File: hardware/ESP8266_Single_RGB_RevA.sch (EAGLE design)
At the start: 41 parts, among them IC1 ESP-12E/F, J1 POWER_JACKPTH_LOCK, J2 B G R +, J4 G S V, Q1 IRF520, Q2 IRF520, Q3 IRF520, T1 2N3904, T2 2N3904, T3 2N3904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

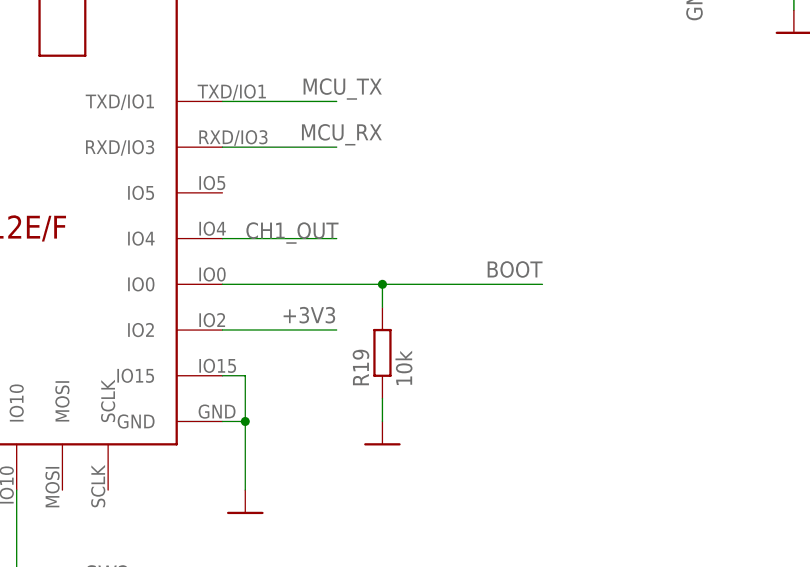
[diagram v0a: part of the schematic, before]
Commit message: fix R16 - NOT NEEDED at ALL
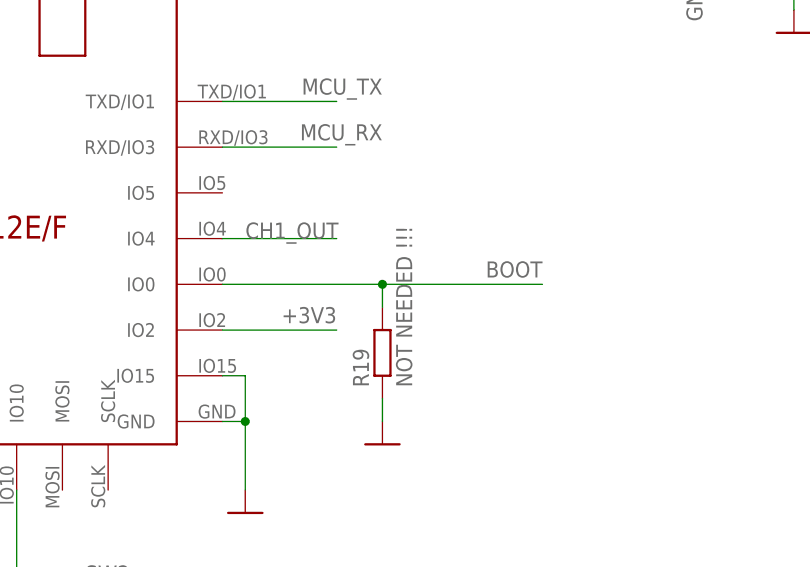
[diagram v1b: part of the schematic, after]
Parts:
- R19: value 10k -> NOT NEEDED !!!
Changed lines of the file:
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@@
 <part name="SV1" library="con-lstb" library_urn="urn:adsk.eagle:library:162" deviceset="MA05-1" device="" package3d_urn="urn:adsk.eagle:package:8332/1" value="GND RX TX BOOT VCC"/>
 <part name="GND31" library="supply1" library_urn="urn:adsk.eagle:library:371" deviceset="GND" device=""/>
-<part name="R19" library="rcl" library_urn="urn:adsk.eagle:library:334" deviceset="R-EU_" device="0207/10" package3d_urn="urn:adsk.eagle:package:23491/2" value="10k"/>
+<part name="R19" library="rcl" library_urn="urn:adsk.eagle:library:334" deviceset="R-EU_" device="0207/10" package3d_urn="urn:adsk.eagle:package:23491/2" value="NOT NEEDED !!!"/>
 <part name="GND32" library="supply1" library_urn="urn:adsk.eagle:library:371" deviceset="GND" device=""/>
 <part name="J2" library="SparkFun-Connectors" deviceset="CONN_04" device="SCREW_LOCK" value="B G R +"/>
